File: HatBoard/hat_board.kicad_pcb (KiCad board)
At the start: 4 copper layers, 106.5 x 99 mm, 108 parts, among them J1 Molex FC Connection, J11 Molex FC Connection, J12 DF11 FC Connection, J17 Molex FC Connection, J18 DF11 FC Connection, J2 DF11 FC Connection, J23 Molex FC Connection, J24 DF11 FC Connection, J29 Molex FC Connection, J3 Conn_01x04, J30 DF11 FC Connection, J35 Molex FC Connection, J36 DF11 FC Connection, J4 Conn_01x04, J5 Conn_01x04, J6 Conn_01x04, J7 Conn_01x04, J8 Conn_01x04, U1 VEML7700, U10 VEML7700, U12 DRV2605LDGS, U13 TCA4311A, U14 VEML7700, U16 DRV2605LDGS, U17 TCA4311A, U18 VEML7700, U2 DRV2605LDGS, U20 DRV2605LDGS, U21 TCA4311A, U22 VEML7700, U24 DRV2605LDGS, U25 TMP112AIDRLR, U26 TMP112AIDRLR, U27 TMP112AIDRLR, U28 TMP112AIDRLR, U29 TMP112AIDRLR, U30 TMP112AIDRLR, U4 TCA4311A, U5 TCA4311A, U6 VEML7700, U8 DRV2605LDGS, U9 TCA4311A

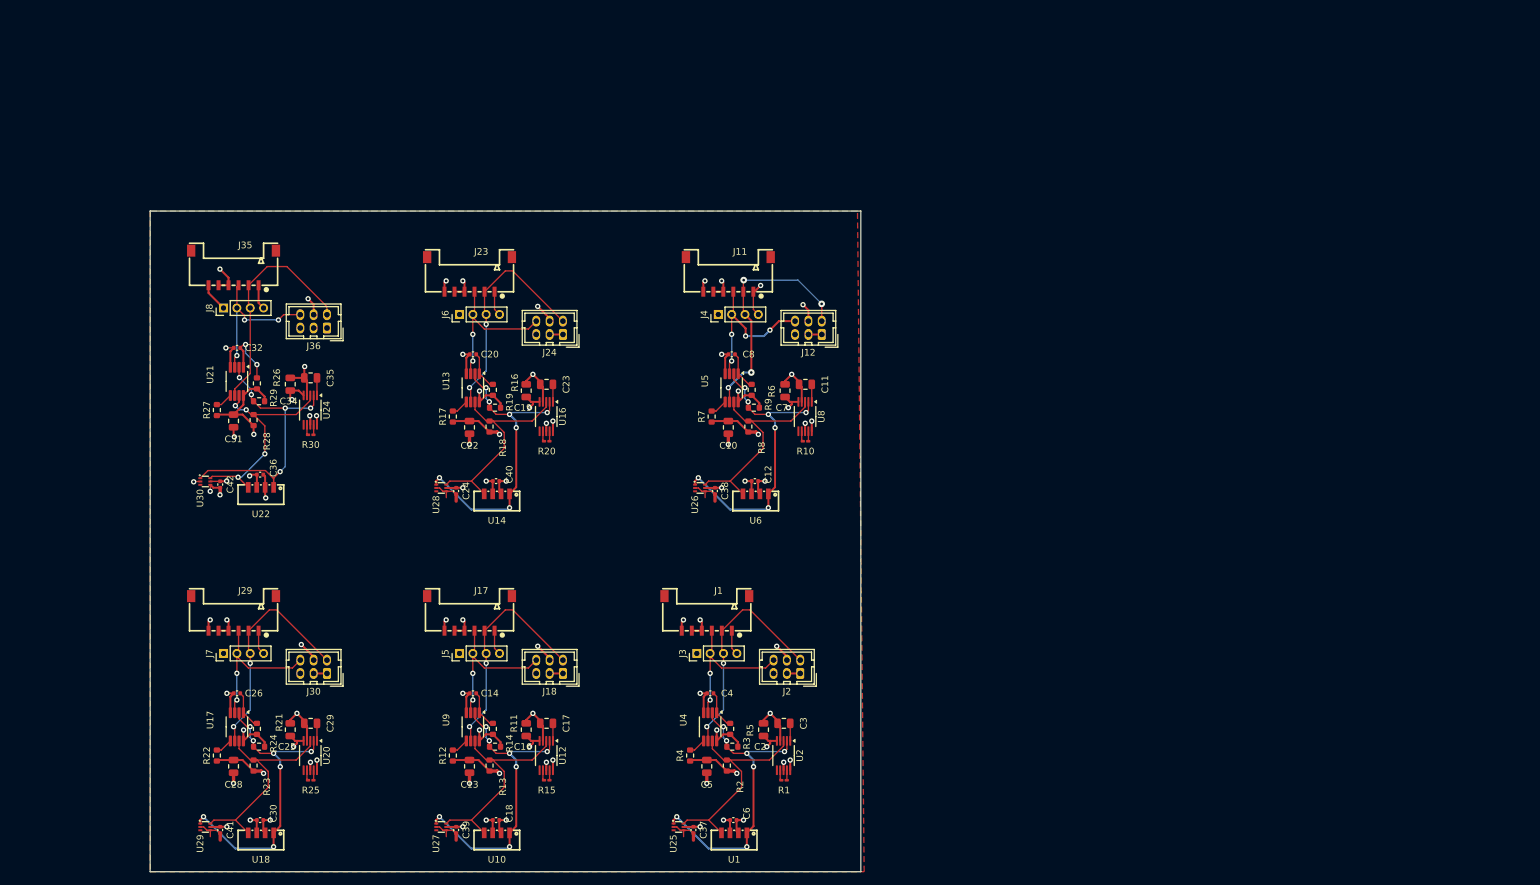
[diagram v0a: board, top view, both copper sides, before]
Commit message: added modifications for 2 cables
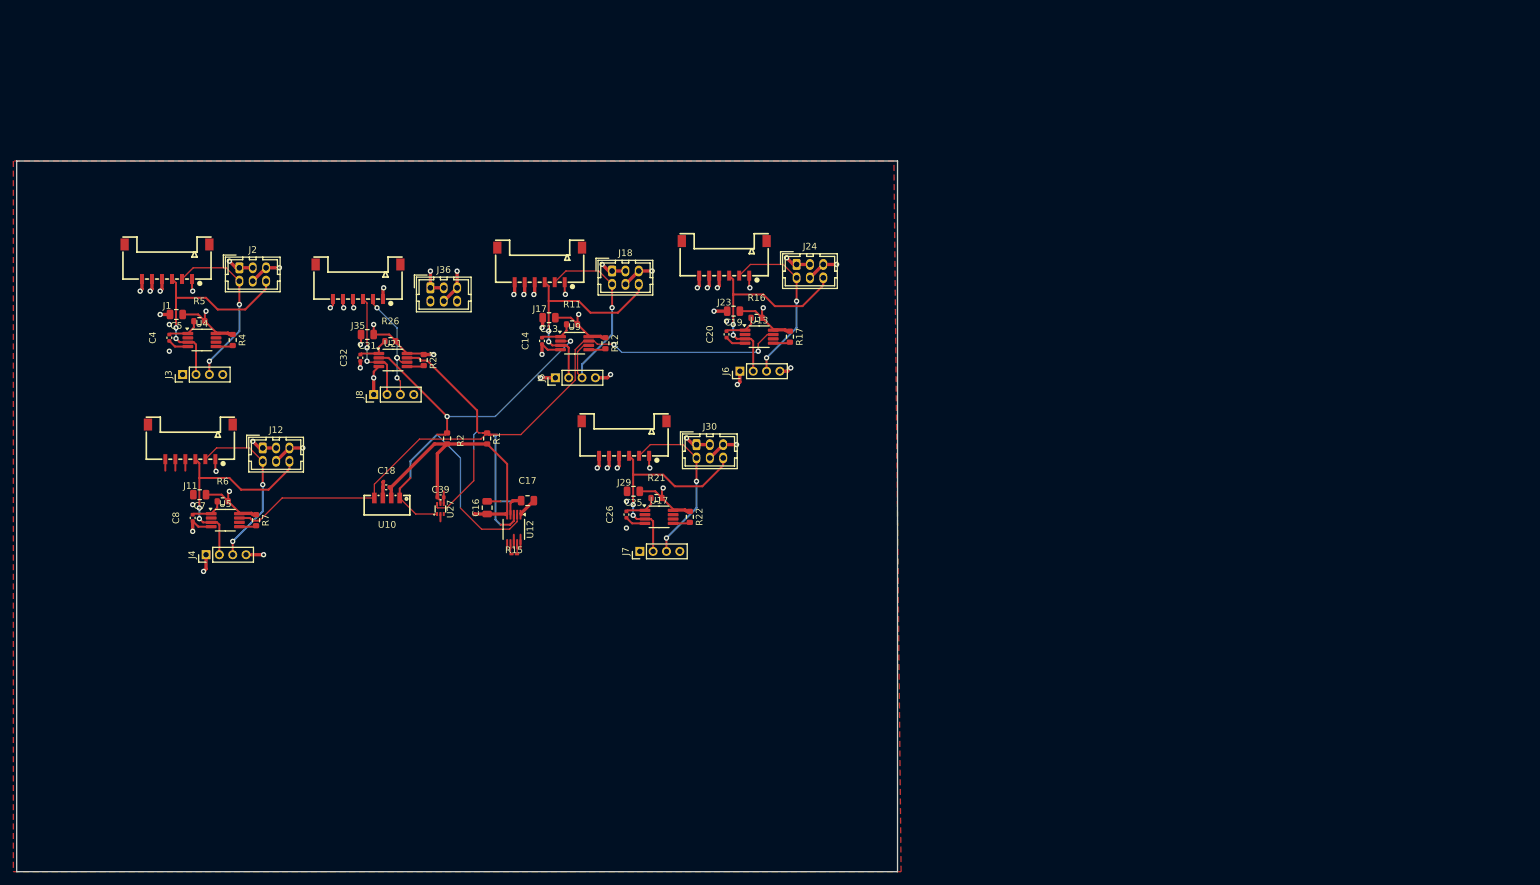
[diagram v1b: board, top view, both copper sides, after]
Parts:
- removed C10, C11, C2, C22, C23, C28, C29, C3, C34, C35: 1uF, Capacitor_SMD:C_0805_2012Metric
- removed C12, C24, C30, C36, C6: 100nF, Capacitor_SMD:C_0402_1005Metric
- removed C37, C38, C40, C41, C42: 10nF, Capacitor_SMD:C_0402_1005Metric
- removed R10, R20, R25, R30: 57.2, Resistor_SMD:R_0201_0603Metric_Pad0.64x0.40mm_HandSolder
- removed R13, R14, R18, R19, R23, R24, R28, R29, R3, R8, R9: 10k, Resistor_SMD:R_0603_1608Metric
- removed U1, U14, U18, U22, U6: VEML7700, easyeda2kicad:SENSOR-SMD_EML7700-TT
- removed U16, U2, U20, U24, U8: DRV2605LDGS, Package_SO:VSSOP-10_3x3mm_P0.5mm
- removed U25, U26, U28, U29, U30: TMP112AIDRLR, easyeda2kicad:SOT-563_L1.6-W1.2-P0.50-LS1.6-BR
- R1: value 57.2 -> 10K; footprint Resistor_SMD:R_0201_0603Metric_Pad0.64x0.40mm_HandSolder -> Resistor_SMD:R_0603_1608Metric
- R2: value 10k -> 10K
- moved C5 104.4 mm to (54.4, 83.0), turned to 180 degrees
- moved J2 103.7 mm to (63.9, 76.0), turned to 0 degrees
- moved R5 100.3 mm to (57.9, 84.0), turned to 180 degrees
- moved C4 97.0 mm to (53.4, 86.5), turned to -90 degrees
- moved J1 96.5 mm to (53.0, 75.1)
- moved U4 95.7 mm to (58.3, 86.8), turned to 0 degrees
- moved R4 92.6 mm to (62.9, 86.8), turned to -90 degrees
- moved C7 89.1 mm to (57.9, 110.0), turned to 180 degrees
- moved J3 87.7 mm to (55.4, 92.0)
- moved J12 85.5 mm to (67.4, 103.0), turned to 0 degrees
- moved J4 84.8 mm to (58.9, 119.0)
- moved J11 84.4 mm to (56.5, 102.1)
- moved C8 84.4 mm to (56.9, 113.5), turned to -90 degrees
- moved R6 81.0 mm to (61.4, 111.0), turned to 180 degrees
- moved R22 79.4 mm to (131.4, 113.3), turned to -90 degrees
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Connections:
- R1 pad 1: Net-(U2-OUT+) -> SDA
- R1 pad 2: Net-(U2-OUT-) -> +3V3
- R2 pad 1: +3V3 -> SCL
- R2 pad 2: /Face Board/SDA -> +3V3
- U10 pad 1: /Face Board2/SCL -> SCL
- U10 pad 4: /Face Board2/SDA -> SDA
- U12 pad 2: /Face Board2/SCL -> SCL
- U12 pad 3: /Face Board2/SDA -> SDA
- U13 pad 2: /Face Board3/SCL -> SCL
- U13 pad 7: /Face Board3/SDA -> SDA
- U17 pad 2: /Face Board4/SCL -> SCL
- U17 pad 7: /Face Board4/SDA -> SDA
- U21 pad 2: /Face Board5/SCL -> SCL
- U21 pad 7: /Face Board5/SDA -> SDA
- U27 pad 1: /Face Board2/SCL -> SCL
- U27 pad 6: /Face Board2/SDA -> SDA
- U4 pad 2: /Face Board/SCL -> SCL
- U4 pad 7: /Face Board/SDA -> SDA
- U5 pad 2: /Face Board1/SCL -> SCL
- U5 pad 7: /Face Board1/SDA -> SDA
- U9 pad 2: /Face Board2/SCL -> SCL
- U9 pad 7: /Face Board2/SDA -> SDA
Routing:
- net SDA: track 0.00 -> 150.4 mm, vias 0 -> 2
- net SCL: track 0.00 -> 84.8 mm, vias 0 -> 2
- net GND: track 178.0 -> 105.0 mm, vias 39 -> 37
- net /Face Board1/SCL: track 46.3 -> 0.00 mm, vias 7 -> 0
- net /Face Board3/SCL: track 46.3 -> 0.00 mm, vias 7 -> 0
- net /Face Board4/SCL: track 46.3 -> 0.00 mm, vias 7 -> 0
- net /Face Board2/SCL: track 46.3 -> 0.00 mm, vias 7 -> 0
- net /Face Board/SCL: track 46.3 -> 0.00 mm, vias 7 -> 0
- net /Face Board5/SCL: track 42.9 -> 0.00 mm, vias 5 -> 0
- net /Face Board5/SDA: track 33.7 -> 0.00 mm, vias 4 -> 0
- net /Face Board3/SDA: track 33.1 -> 0.00 mm
- net /Face Board1/SDA: track 33.1 -> 0.00 mm
- net /Face Board2/SDA: track 33.1 -> 0.00 mm
- net /Face Board/SDA: track 33.1 -> 0.00 mm
- net /Face Board4/SDA: track 33.1 -> 0.00 mm
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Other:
- board size 106.5 x 99 mm -> 132 x 106.5 mm

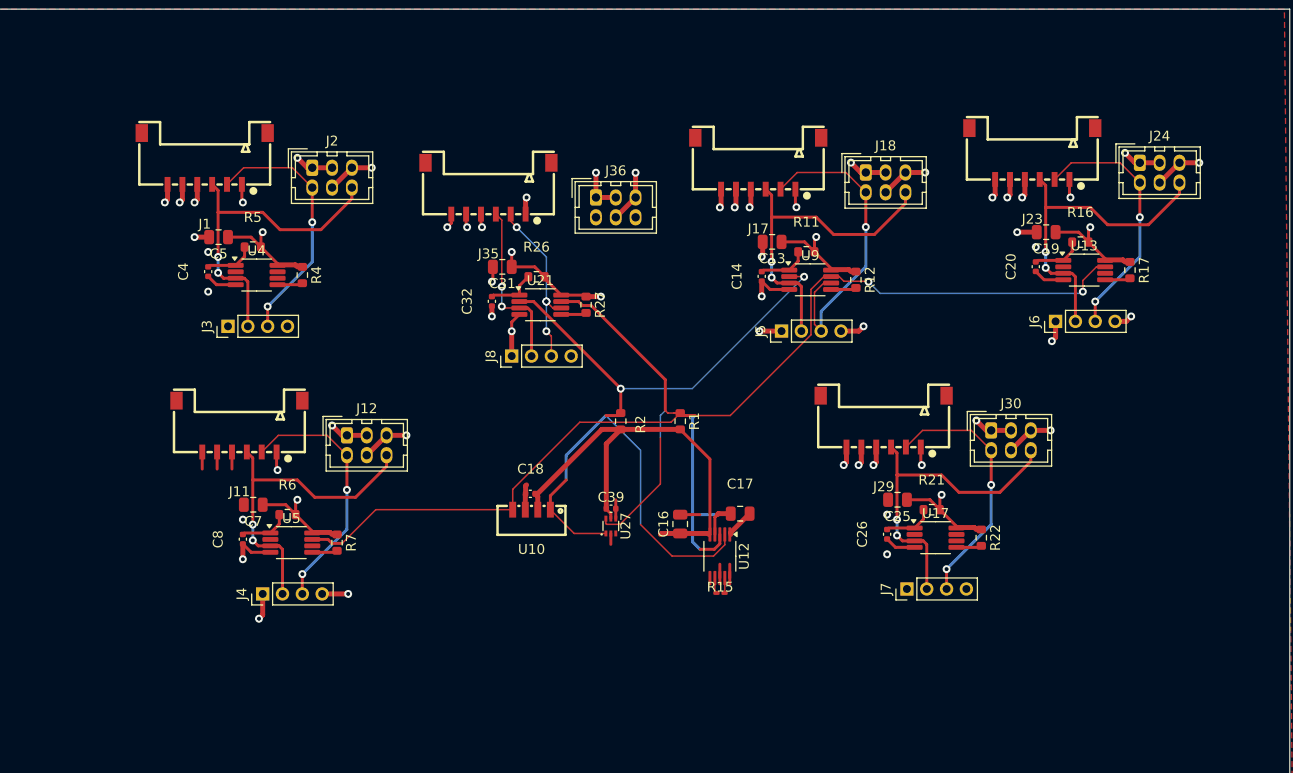
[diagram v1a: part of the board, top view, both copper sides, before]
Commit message: placement for face baord attachment
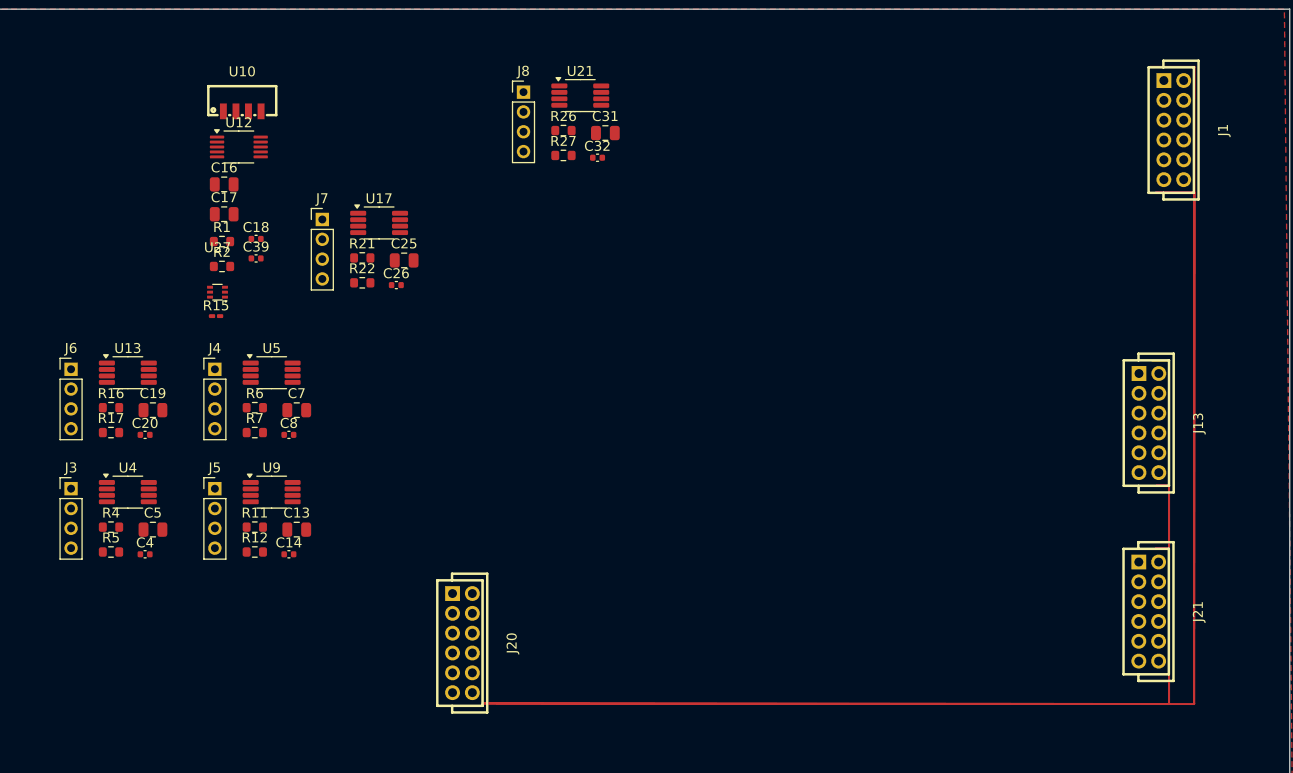
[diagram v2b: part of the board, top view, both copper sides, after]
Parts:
- removed J11, J17, J23, J29, J35: Molex FC Connection, easyeda2kicad:CONN-SMD_6P-P1.50_A1501WRB-S-6P
- removed J12, J18, J2, J24, J30, J36: DF11 FC Connection, Connector_Hirose:Hirose_DF11-6DP-2DSA_2x03_P2.00mm_Vertical
- added J13: DF11 FC Connection, easyeda2kicad:CONN-TH_DF11-12DS-2DSA-05, F.Cu at (148.3, 101.8)
- added J20: DF11 FC Connection, easyeda2kicad:CONN-TH_DF11-12DS-2DSA-05, F.Cu at (79.0, 124.0)
- added J21: DF11 FC Connection, easyeda2kicad:CONN-TH_DF11-12DS-2DSA-05, F.Cu at (148.3, 120.8)
- J1: value Molex FC Connection -> DF11 FC Connection; footprint easyeda2kicad:CONN-SMD_6P-P1.50_A1501WRB-S-6P -> easyeda2kicad:CONN-TH_DF11-12DS-2DSA-05
- moved R17 104.1 mm to (43.6, 102.7), turned to 0 degrees
- moved J6 99.5 mm to (39.5, 96.3), turned to 0 degrees
- moved R16 99.2 mm to (43.6, 100.2), turned to 0 degrees
- moved J1 97.8 mm to (150.8, 72.2), turned to -90 degrees
- moved U13 97.0 mm to (45.3, 96.7)
- moved C19 91.9 mm to (47.8, 100.5), turned to 0 degrees
- moved C20 91.5 mm to (47.0, 103.0), turned to 0 degrees
- moved J7 69.8 mm to (64.9, 81.2), turned to 0 degrees
- moved R22 67.5 mm to (68.9, 87.6), turned to 0 degrees
- moved R12 66.6 mm to (58.1, 114.8), turned to 0 degrees
- moved U17 64.5 mm to (70.6, 81.6)
- moved U12 63.7 mm to (56.5, 73.9), turned to 0 degrees
- moved R21 62.8 mm to (68.9, 85.1), turned to 0 degrees
- moved R11 62.2 mm to (58.1, 112.3), turned to 0 degrees
- moved C17 60.2 mm to (55.0, 80.7), turned to 0 degrees
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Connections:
- net /Face Board1/SCLIN renamed /SCLIN_F2
- net /Face Board1/SDAIN renamed /SDAIN_F2
- net /Face Board2/SCLIN renamed /SCLIN_F3
- net /Face Board2/SDAIN renamed /SDAIN_F3
- net /Face Board3/SCLIN renamed /SCLIN_F4
- net /Face Board3/SDAIN renamed /SCDAIN_F4
- J1 pad 2: /Face Board/SDAIN -> GND
- J1 pad 3: /Face Board/SCLIN -> unconnected-(J1-Pin_3-Pad3)
- J1 pad 4: +3V3 -> unconnected-(J1-Pin_4-Pad4)
- J1 pad 5: +3V3 -> unconnected-(J1-Pin_5-Pad5)
- J1 pad 6: GND -> /SCLIN
- J1 pad 7: (no net) -> +3V3
- J1 pad 8: (no net) -> /SDAIN
- J3 pad 2: /Face Board/SCLIN -> /SCLIN_F1
- J3 pad 3: /Face Board/SDAIN -> /SDAIN_F1
- J7 pad 2: /Face Board4/SCLIN -> /SCLIN
- J7 pad 3: /Face Board4/SDAIN -> /SDAIN
- J8 pad 2: /Face Board5/SCLIN -> /SDAIN
- J8 pad 3: /Face Board5/SDAIN -> /SCLIN
- U17 pad 3: /Face Board4/SCLIN -> /SCLIN
- U17 pad 6: /Face Board4/SDAIN -> /SDAIN
- U21 pad 3: /Face Board5/SCLIN -> /SDAIN
- U21 pad 6: /Face Board5/SDAIN -> /SCLIN
- U4 pad 3: /Face Board/SCLIN -> /SCLIN_F1
- U4 pad 6: /Face Board/SDAIN -> /SDAIN_F1
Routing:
- net +3V3: track 162.1 -> 0.00 mm, vias 23 -> 0
- net SDA: track 150.4 -> 0.00 mm, vias 2 -> 0
- net GND: track 105.0 -> 0.00 mm, vias 37 -> 0
- net SCL: track 84.8 -> 0.00 mm, vias 2 -> 0
- net /Face Board/SCLIN: track 33.7 -> 0.00 mm, vias 2 -> 0
- net /SCLIN_F2: track 33.7 -> 0.00 mm, vias 2 -> 0
- net /Face Board4/SCLIN: track 33.7 -> 0.00 mm, vias 2 -> 0
- net /SCLIN_F4: track 33.7 -> 0.00 mm, vias 2 -> 0
- net /SCLIN_F3: track 33.7 -> 0.00 mm, vias 2 -> 0
- net /SDAIN_F3: track 32.2 -> 0.00 mm, vias 1 -> 0
- net /SDAIN_F2: track 26.0 -> 0.00 mm, vias 2 -> 0
- net /Face Board/SDAIN: track 26.0 -> 0.00 mm, vias 2 -> 0
- net /Face Board4/SDAIN: track 26.0 -> 0.00 mm, vias 2 -> 0
- net /SCDAIN_F4: track 26.0 -> 0.00 mm, vias 2 -> 0
- net /Face Board5/SDAIN: track 17.8 -> 0.00 mm, vias 4 -> 0
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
